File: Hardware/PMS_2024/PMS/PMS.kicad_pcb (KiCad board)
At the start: 2 copper layers, 185.9 x 135.1 mm, 106 parts, among them J1 RJ45_LED_Shielded, Q1 BSS138, Q2 BSS138, Q3 SPD30P06PGBTMA1, Q4 BSS138, Q5 SPD30P06PGBTMA1, Q6 BSS138, Q7 IPB180N10S4-02, U1 Teensy4.1_DEV-16771, U2 PKE3316ZPI, U3 PKE3316ZPI, U4 ACS758xCB-200B-PFF, U5 Opamp_Dual, U6 OKI, U7 Opamp_Dual, U8 ACS725xLCTR-20AB, U9 Opamp_Dual

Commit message: Finished General Layout
All trace work still needs to be done
General layout is finished
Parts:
- moved C1 264.8 mm to (77.5, 124.5), turned to -90 degrees
- moved D4 260.9 mm to (56.4, 31.8)
- moved D5 260.9 mm to (56.4, 35.1)
- moved D6 260.8 mm to (56.4, 38.4)
- moved D7 260.7 mm to (56.4, 41.7)
- moved D8 260.7 mm to (56.4, 45.0)
- moved D9 260.6 mm to (56.4, 48.3)
- moved D1 260.0 mm to (56.4, 51.6)
- moved C4 234.4 mm to (99.1, 84.3), turned to 90 degrees
- moved R41 230.7 mm to (61.0, 45.0)
- moved R42 230.6 mm to (61.0, 48.3)
- moved BZ1 217.1 mm to (107.8, 100.8)
- moved R7 217.1 mm to (61.0, 41.7)
- moved U6 217.0 mm to (115.6, 125.1)
- moved R4 216.8 mm to (61.0, 31.8)
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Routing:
- net cell6: track 0.00 -> 8.78 mm
- net cell1: track 0.00 -> 8.78 mm
- net cell5: track 0.00 -> 8.57 mm
- net cell2: track 0.00 -> 8.57 mm
- net cell4: track 0.00 -> 8.36 mm
- net cell3: track 0.00 -> 8.36 mm
- added copper zone on F.Cu, net LowCurrent_PWR
- added copper zone on F.Cu, net Motor_PWR

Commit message: Changed Layout
Changed the entire layout
Most traces still need to be routed
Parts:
- removed R2: 1.0K, Resistor_SMD:R_0603_1608Metric_Pad0.98x0.95mm_HandSolder
- BZ1: footprint MRDT_Devices:BUZZER_SMI_1324_TW_5V_2_R -> Buzzer_Beeper:Buzzer_12x9.5RM7.6
- Conn16: footprint MRDT_Connectors:Square_Anderson_2_H_Stacked -> MRDT_Connectors:Square_Anderson_2_H_Side_By_Side_PV
- moved J1 174.2 mm to (273.2, 83.5), turned to 180 degrees
- moved C3 146.8 mm to (267.2, 109.5), turned to 90 degrees
- moved Q7 130.7 mm to (173.2, 170.0), turned to -90 degrees
- moved C11 129.1 mm to (233.7, 118.9)
- moved C13 129.1 mm to (233.7, 122.2)
- moved BZ1 126.9 mm to (234.2, 89.7), turned to -90 degrees
- moved R27 125.6 mm to (285.5, 171.7), turned to 90 degrees
- moved U4 121.9 mm to (233.6, 154.0), turned to 90 degrees
- moved R30 120.8 mm to (285.5, 167.4), turned to 90 degrees
- moved R32 120.4 mm to (277.1, 175.8)
- moved R28 120.3 mm to (288.5, 171.7), turned to 90 degrees
- moved U9 119.6 mm to (279.4, 170.7), turned to 0 degrees
- moved R29 119.5 mm to (288.5, 167.4), turned to -90 degrees
- moved R31 116.4 mm to (273.3, 171.8), turned to 90 degrees
- moved C10 115.7 mm to (101.1, 146.4)
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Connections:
- C13 pad 1: +3V3 -> +3.3V
- U1 pad 3.3V_1: +3V3 -> +3.3V
- U1 pad 3.3V_2: +3V3 -> +3.3V
- U4 pad 4: +BATT -> PV
- U4 pad 5: PV -> +BATT
- U8 pad 8: +3V3 -> +3.3V
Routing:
- net +3.3V: track 0.00 -> 575.6 mm
- net PV: track 0.00 -> 112.0 mm, vias 0 -> 4
- net Cell5-SENSE: track 0.00 -> 67.5 mm
- net cell1: track 8.78 -> 47.6 mm
- net cell3: track 8.36 -> 44.8 mm
- net cell2: track 8.57 -> 42.0 mm
- net cell5: track 8.57 -> 39.1 mm
- net cell4: track 8.36 -> 35.4 mm, vias 0 -> 2
- net LowCurrent_Enable: track 0.00 -> 20.7 mm, vias 0 -> 1
- net Net-(Q5-G): track 0.00 -> 18.2 mm
- net Buzzer: track 0.00 -> 16.7 mm
- net Net-(U7A--): track 0.00 -> 11.9 mm
- net Net-(U9A--): track 0.00 -> 11.8 mm
- net Net-(U5A--): track 0.00 -> 11.5 mm
- net Net-(U7A-+): track 0.00 -> 9.21 mm
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- added copper zone on F.Cu, net Aux_PWR
- added copper zone on F.Cu, net NS_24V
- added copper zone on F.Cu, net Net-(Q3-D)
- added copper zone on F.Cu, net POE_24V
- removed copper zone on B.Cu, net +BATT
- removed copper zone on B.Cu, net PV
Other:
- board size 185.9 x 135.1 mm -> 224 x 109.7 mm

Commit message: Finished Layout + Traces
Finished Layout
Silkscreens still need to be added
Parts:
- Conn16: moved to B.Cu
- moved R5 153.2 mm to (119.6, 190.5), turned to 90 degrees
- moved D5 151.6 mm to (123.4, 191.5), turned to 180 degrees
- moved R6 131.7 mm to (76.2, 140.7), turned to -90 degrees
- moved D6 125.2 mm to (76.2, 136.1), turned to -90 degrees
- moved D4 107.9 mm to (239.5, 122.4), turned to 90 degrees
- moved R4 101.4 mm to (239.5, 117.9), turned to 90 degrees
- moved R41 85.3 mm to (96.6, 97.5)
- moved D8 85.3 mm to (92.1, 97.5)
- moved D1 82.4 mm to (239.5, 101.1), turned to -90 degrees
- moved R3 80.7 mm to (239.5, 105.7), turned to -90 degrees
- moved D9 53.0 mm to (129.8, 97.5)
- moved R42 53.0 mm to (134.4, 97.5)
- moved D7 47.6 mm to (182.9, 97.5)
- moved R7 47.6 mm to (187.5, 97.5)
- moved Conn16 33.9 mm to (225.9, 177.0)
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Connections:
- U1 pad 0: Motor_Enable -> POE_Enable
- U1 pad 1: Aux_Enable -> NS_Enable
- U1 pad 11: NS_Enable -> unconnected-(U1-MOSI-Pad11)
- U1 pad 12: POE_Enable -> unconnected-(U1-MISO-Pad12)
- U1 pad 14: Cell3-SENSE -> Cell5-SENSE
- U1 pad 15: Cell4-SENSE -> Cell6-SENSE
- U1 pad 16: CS_Aux -> Cell3-SENSE
- U1 pad 17: unconnected-(U1-A3-Pad17) -> Cell4-SENSE
- U1 pad 27: CS1 -> CS_Aux
- U1 pad 31: unconnected-(U1-CTX3-Pad31) -> Aux_Enable
- U1 pad 32: unconnected-(U1-OUT1B-Pad32) -> Motor_Enable
- U1 pad 38: CS2 -> unconnected-(U1-A14-Pad38)
- U1 pad 39: CS3 -> CS1
- U1 pad 40: Cell5-SENSE -> CS2
- U1 pad 41: Cell6-SENSE -> CS3
- U1 pad 7: LowCurrent_Enable -> Buzzer
- U1 pad 8: Buzzer -> LowCurrent_Enable
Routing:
- net CS_Aux: track 0.00 -> 263.2 mm, vias 0 -> 1
- net POE_Enable: track 0.00 -> 195.1 mm
- net Aux_Enable: track 3.22 -> 177.1 mm, vias 0 -> 1
- net NS_Enable: track 0.00 -> 156.2 mm
- net Motor_Enable: track 0.00 -> 91.1 mm, vias 0 -> 2
- net Cell2-SENSE: track 5.80 -> 82.7 mm, vias 0 -> 1
- net Cell6-SENSE: track 5.28 -> 74.7 mm, vias 0 -> 1
- net Cell3-SENSE: track 4.48 -> 71.9 mm, vias 0 -> 1
- net Cell1-SENSE: track 4.48 -> 68.5 mm, vias 0 -> 1
- net Cell4-SENSE: track 5.32 -> 65.7 mm, vias 0 -> 1
- net CS1: track 0.00 -> 41.5 mm
- net CURRENT_SENSE: track 0.00 -> 34.2 mm
- net CS2: track 0.00 -> 28.2 mm
- net +3.3V: track 575.6 -> 603.8 mm
- net LED: track 0.00 -> 27.9 mm
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
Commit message: Added Silkscreens
Added Signature and Silkscreens
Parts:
- added G***: LOGO, Signatures:Jorge_Noriega_30mmx13.8mm, F.Cu at (111.1, 159.1)
- added G***: LOGO, MRDT_Silkscreens:0_MRDT_Logo_20mm, F.Cu at (144.9, 150.9)
- moved C10 81.9 mm to (182.4, 136.5)
- moved D2 47.2 mm to (109.7, 136.4), turned to 180 degrees
- moved C5 42.1 mm to (172.2, 131.2)
- moved C7 42.1 mm to (192.3, 131.2)
- moved C9 42.1 mm to (212.3, 131.2)
- moved C8 42.1 mm to (152.4, 131.3)
- moved D3 28.3 mm to (121.3, 136.4), turned to 180 degrees
- moved R6 2.55 mm to (78.7, 140.5), turned to 0 degrees
- moved R7 1.82 mm to (187.1, 99.3), turned to -90 degrees
- moved D6 1.70 mm to (77.7, 136.9)
- moved D7 1.00 mm to (183.5, 98.3)
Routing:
- net Motor_Enable: track 91.1 -> 81.0 mm
- net LowCurrent_PWR: track 6.39 -> 0.00 mm
- net Aux_PWR: track 4.47 -> 0.00 mm
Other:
- board text added: "+Battery-"
- board text added: "3.3V"
- board text added: "AUX"
- board text added: "CS1"
- board text added: "CS2"
- board text added: "CS3"
- board text added: "Low Current Ports"
- board text added: "Motor Ports"
- board text added: "NS"
- board text added: "POE"
- board text added: "Power Management System Mars Rover Design Team Missouri S&T, 2024 Jorge Noriega"

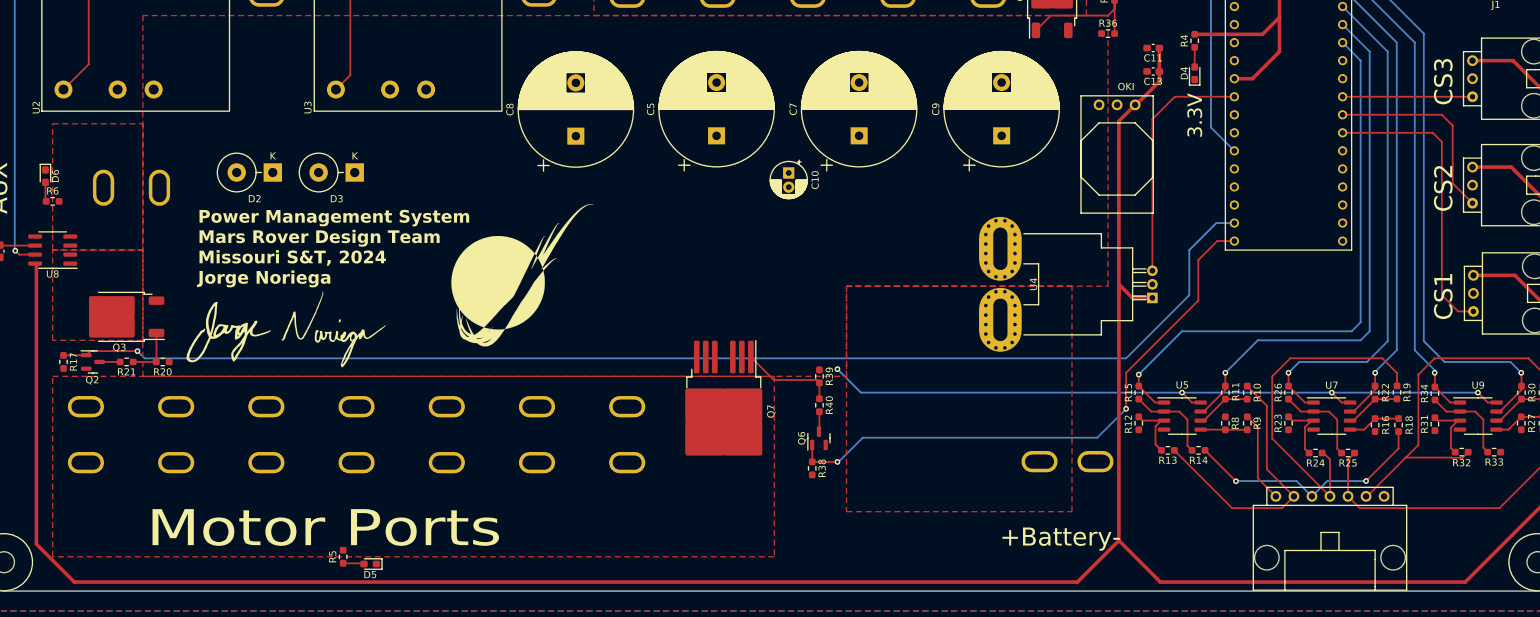
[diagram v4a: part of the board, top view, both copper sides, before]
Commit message: Layout Changes
Added SL labels
Moved some traces, away from planes
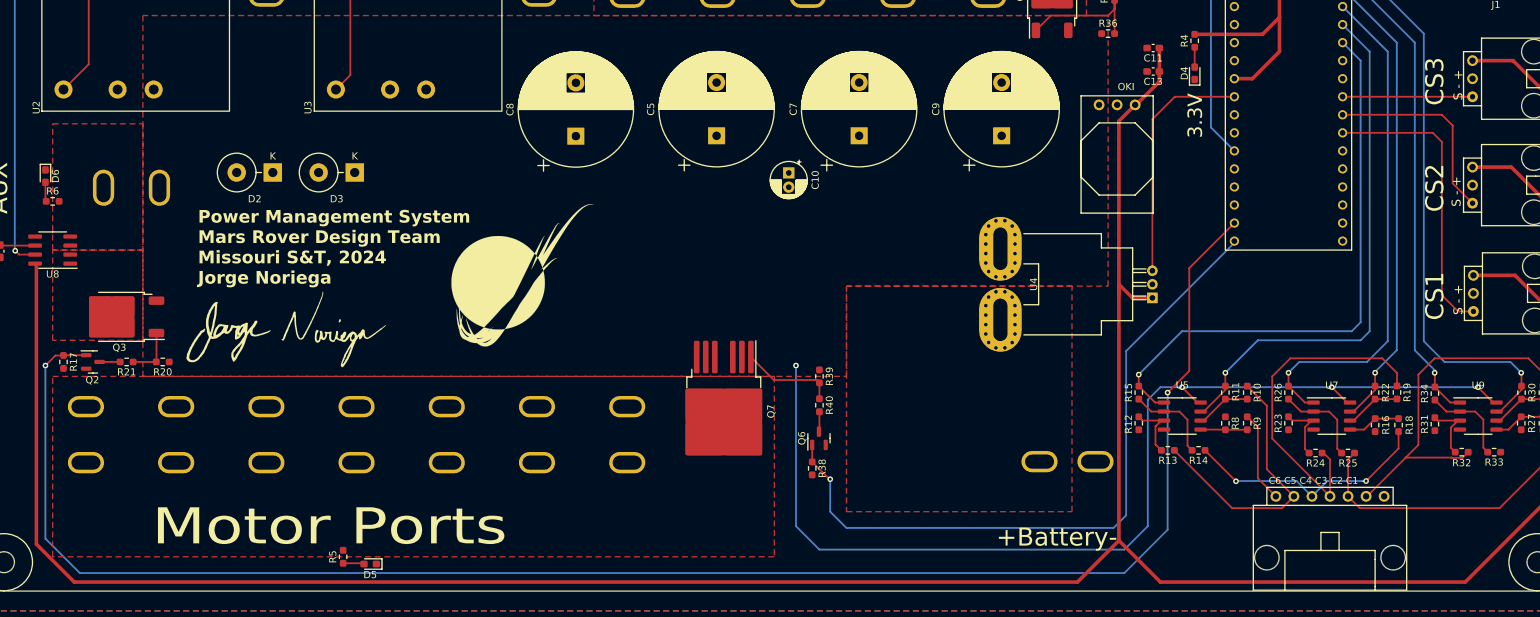
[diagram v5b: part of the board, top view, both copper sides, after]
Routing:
- net Aux_Enable: track 177.1 -> 240.3 mm, vias 1 -> 2
- net PV: track 101.1 -> 150.3 mm
- net Motor_Enable: track 81.0 -> 98.8 mm, vias 2 -> 1
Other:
- board text added: "C6 C5 C4 C3 C2 C1 -"
- board text added: "S - +"

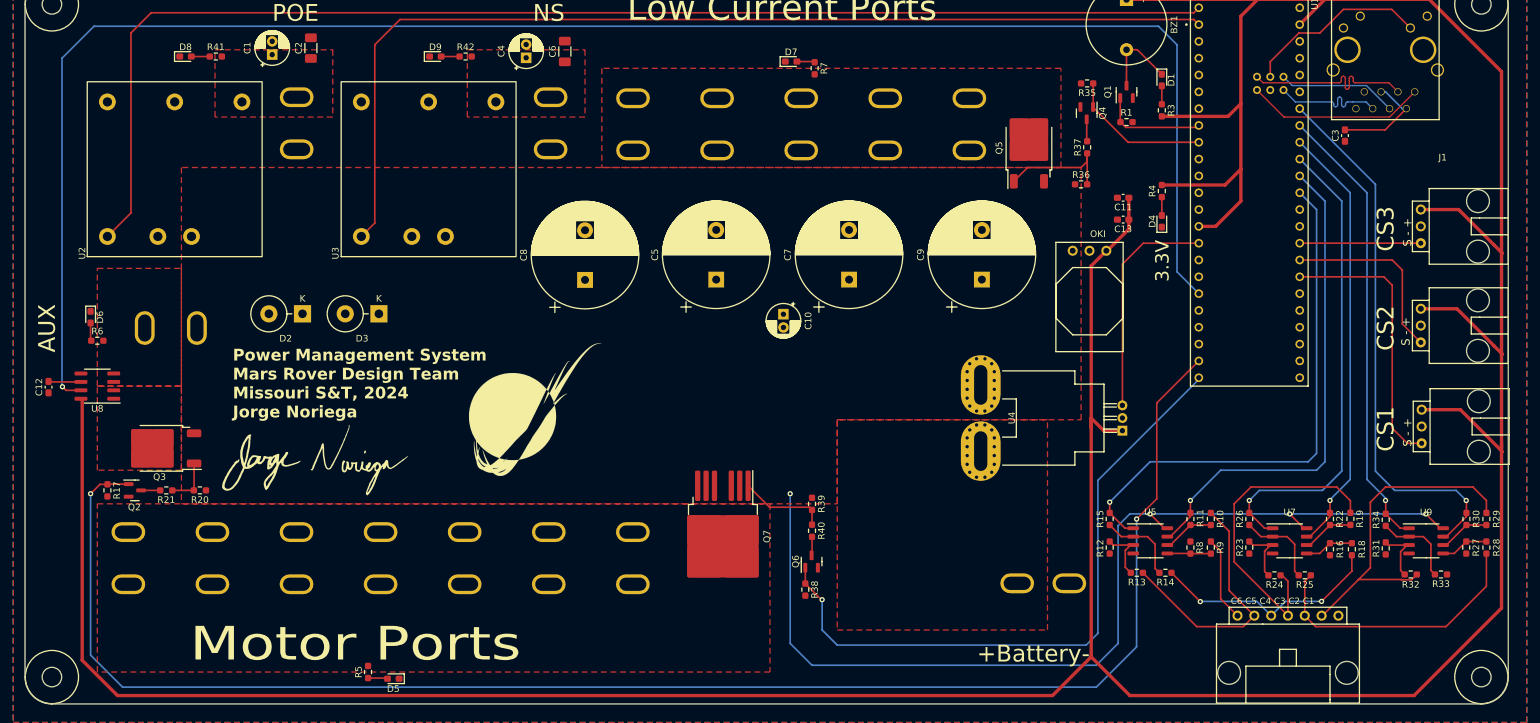
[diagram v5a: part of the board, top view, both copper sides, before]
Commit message: Resistor Changes
Added a PV LED
Changed some resistor values
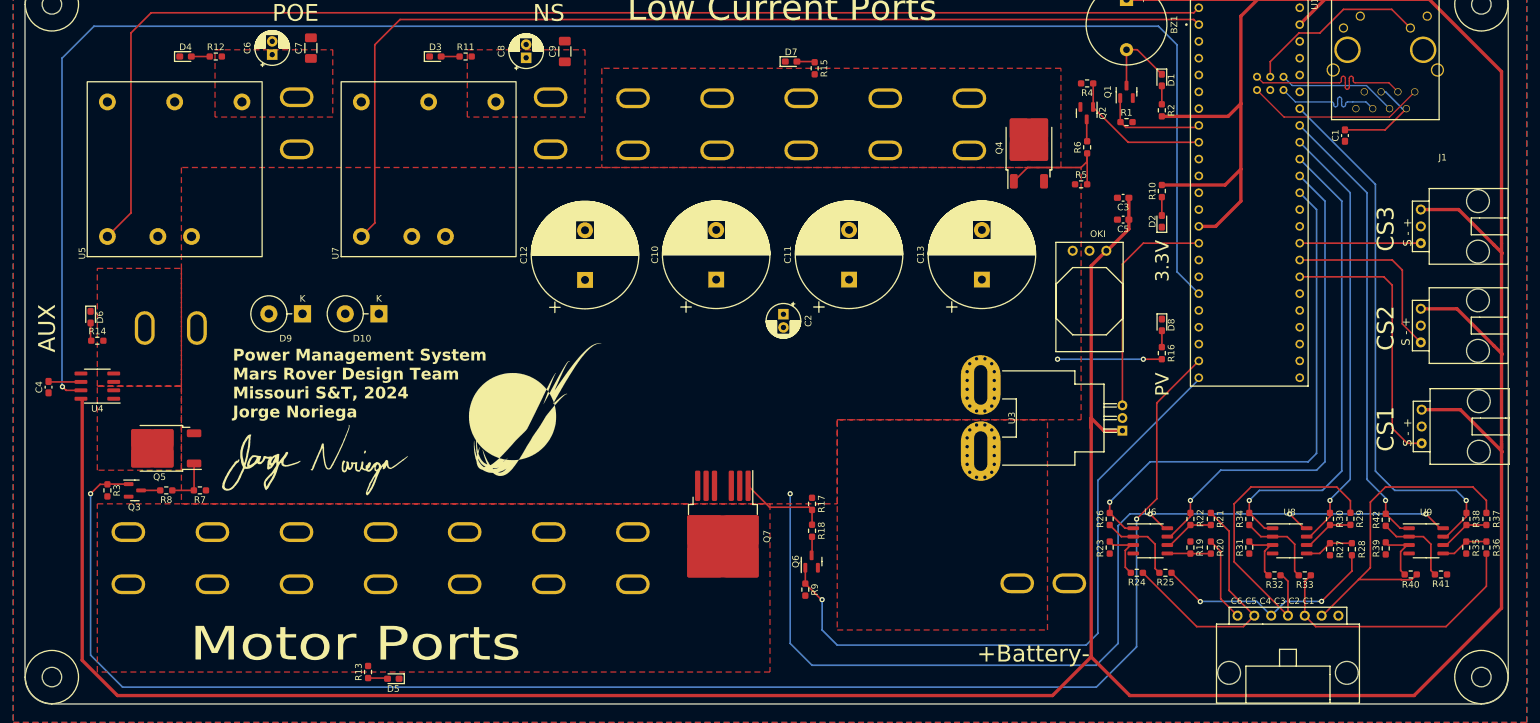
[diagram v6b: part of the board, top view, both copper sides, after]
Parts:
- added D8: Green, LED_SMD:LED_0603_1608Metric_Pad1.05x0.95mm_HandSolder, F.Cu at (239.5, 138.1)
- added R16: 2k, Resistor_SMD:R_0603_1608Metric_Pad0.98x0.95mm_HandSolder, F.Cu at (239.5, 142.3)
- R13: renamed from R5; value 3k -> 2k
- R14: renamed from R6; value 3k -> 2k
- R15: renamed from R7; value 3k -> 2k
- renumbered C3 to C1, C5 to C10, C7 to C11, C8 to C12, C9 to C13, C10 to C2, C11 to C3, C12 to C4, C13 to C5, C1 to C6, C2 to C7, C4 to C8, C6 to C9, Conn20 to Conn17, Conn19 to Conn18, Conn18 to Conn19, Conn17 to Conn20, D3 to D10, D4 to D2, D9 to D3, D8 to D4, D2 to D9, Q4 to Q2, Q2 to Q3, Q5 to Q4, Q3 to Q5, R4 to R10, R42 to R11, R41 to R12, R39 to R17, R40 to R18, R8 to R19, R3 to R2, R9 to R20, R10 to R21, R11 to R22, R12 to R23, R13 to R24, R14 to R25, R15 to R26, R16 to R27, R18 to R28, R19 to R29, R17 to R3, R22 to R30, R23 to R31, R24 to R32, R25 to R33, R26 to R34, R27 to R35, R28 to R36, R29 to R37, R30 to R38, R31 to R39, R35 to R4, R32 to R40, R33 to R41, R34 to R42, R36 to R5, R37 to R6, R20 to R7, R21 to R8, R38 to R9, U6 to U2, U4 to U3, U8 to U4, U2 to U5, U5 to U6, U3 to U7, U7 to U8
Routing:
- net PV: track 150.3 -> 166.1 mm, vias 4 -> 6
- net Net-(D8-A): track 0.00 -> 2.49 mm
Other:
- board text added: "PV"

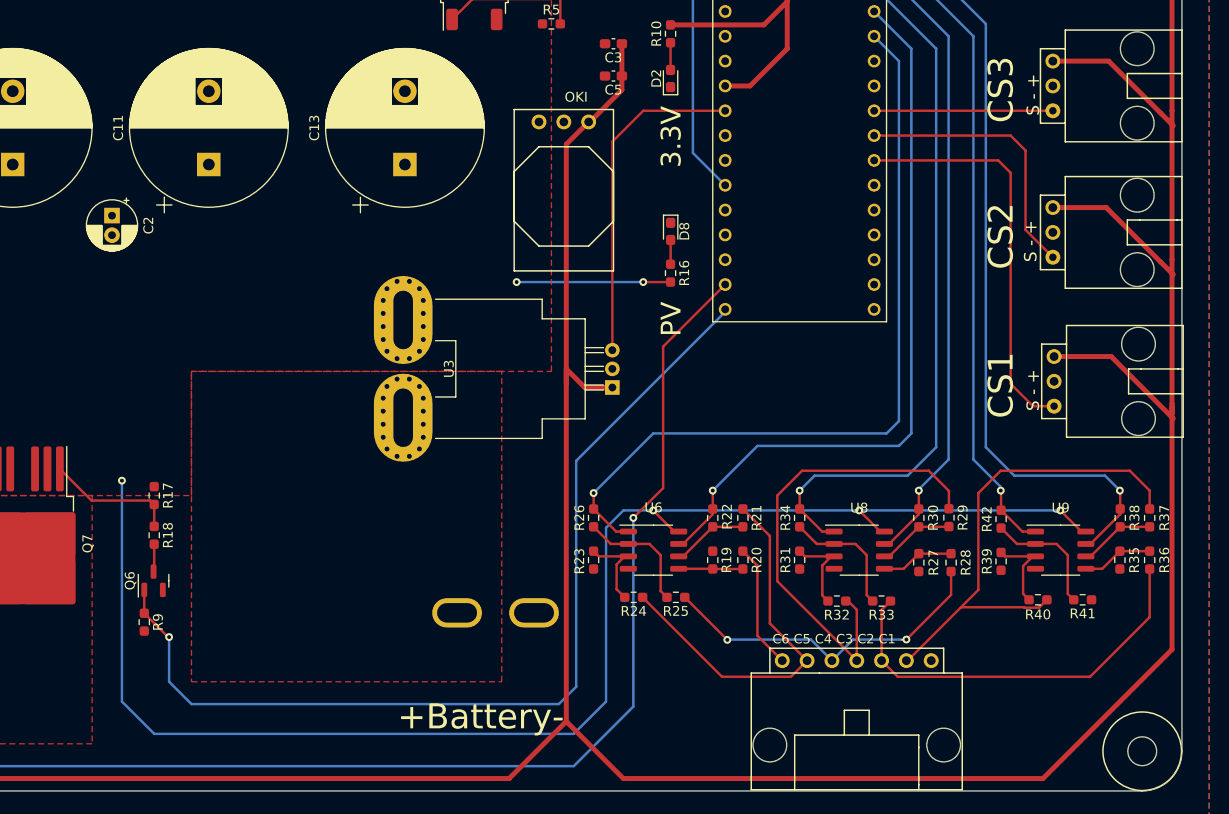
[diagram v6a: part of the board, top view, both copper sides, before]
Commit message: Trace change
Moved trace for a wider GND plane
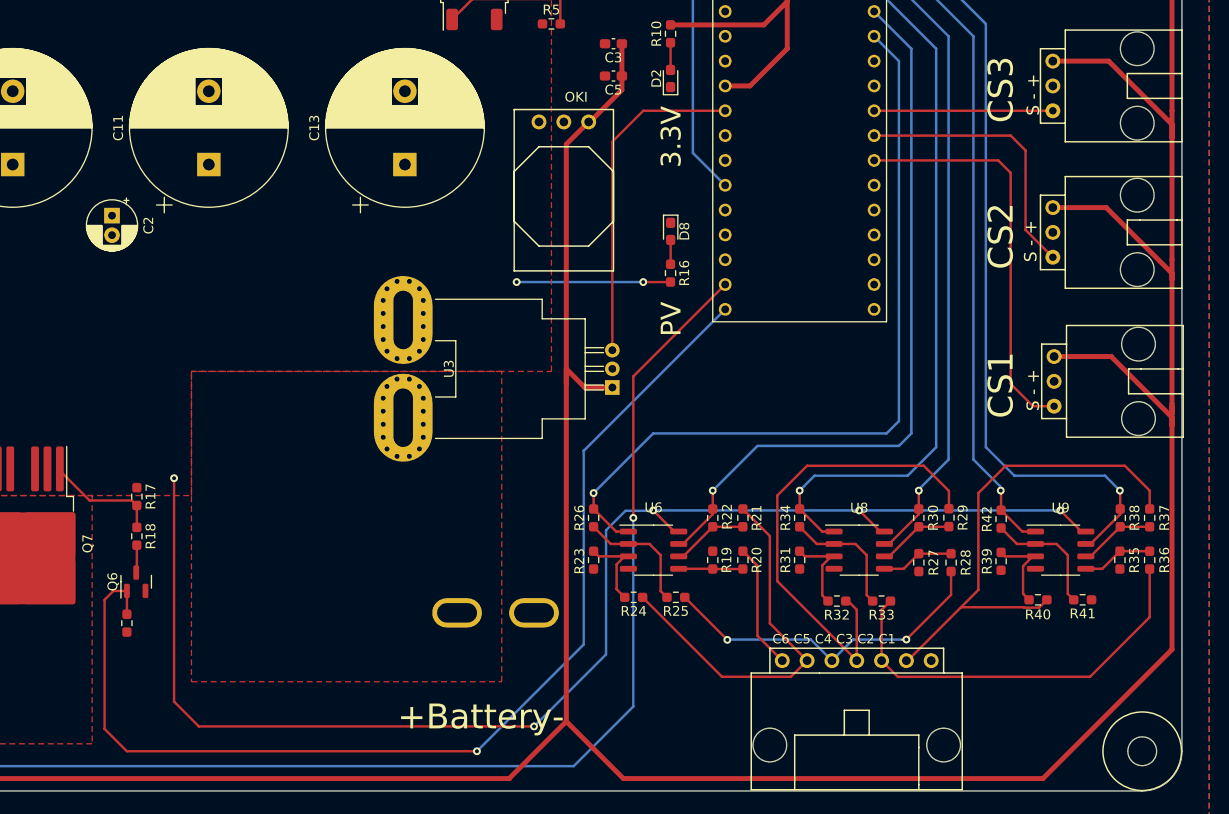
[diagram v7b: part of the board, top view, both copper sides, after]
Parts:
- moved R9 1.78 mm to (183.9, 178.2)
- moved R18 1.78 mm to (184.9, 169.3)
- moved Q6 1.78 mm to (184.8, 173.9)
- moved R17 1.78 mm to (184.9, 165.2)
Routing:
- net Motor_Enable: track 98.8 -> 113.0 mm
- net PV: track 166.1 -> 157.4 mm, vias 6 -> 7
- net +3.3V: track 603.8 -> 606.2 mm
- net Net-(Q7-G): track 13.4 -> 11.8 mm

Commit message: Footprint Change
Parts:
- C2: footprint Capacitor_THT:CP_Radial_D5.0mm_P2.00mm -> Capacitor_SMD:C_1206_3216Metric_Pad1.33x1.80mm_HandSolder
- C3: value 10uF -> 22uF
- moved C2 47.4 mm to (227.3, 121.4), turned to 0 degrees
- moved G*** 4.00 mm to (114.8, 160.6)
- moved G*** 4.00 mm to (148.6, 152.4)
